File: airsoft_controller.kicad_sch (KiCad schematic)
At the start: 31 parts, among them J1 Micro_SD_Card, SW1 MEMBRANE, SW2 MEMBRANE, SW3 MECH_SW, SW4 MEMBRANE, SW5 MEMBRANE, SW6 MEMBRANE, SW7 MEMBRANE, U1 CP2102N-Axx-xQFN20, U2 ESP32-S3-WROOM-1, U3 74HC595, U8 SN74HCS165

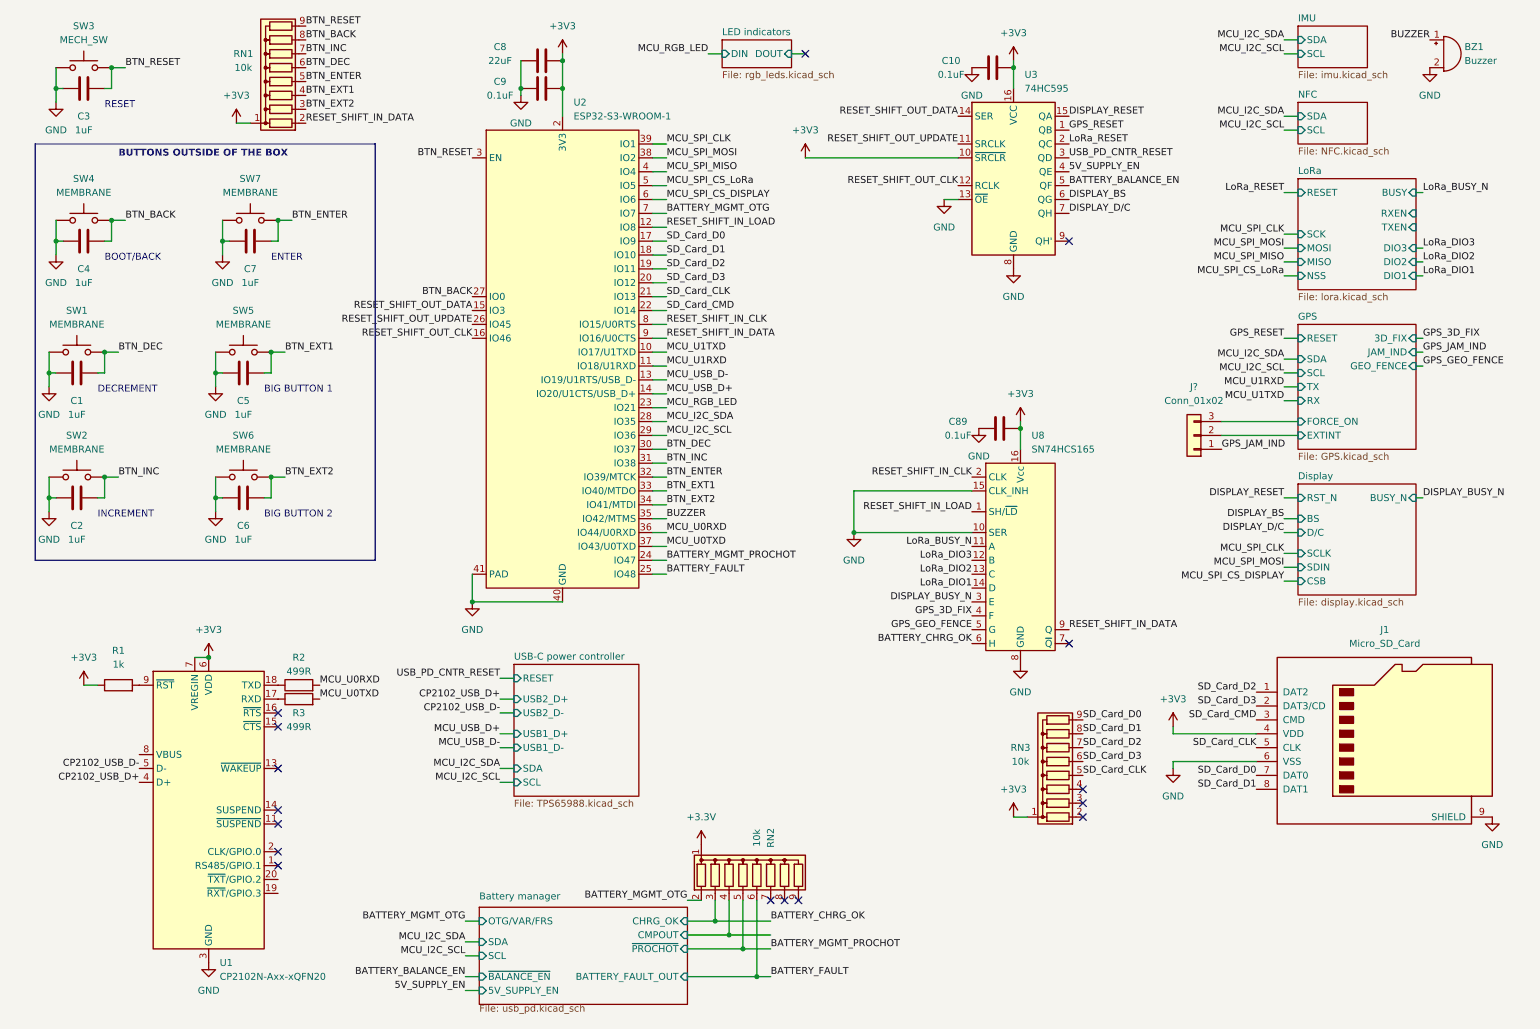
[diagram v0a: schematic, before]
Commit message: minor optimized pinassignement, added capacitors, added connectors
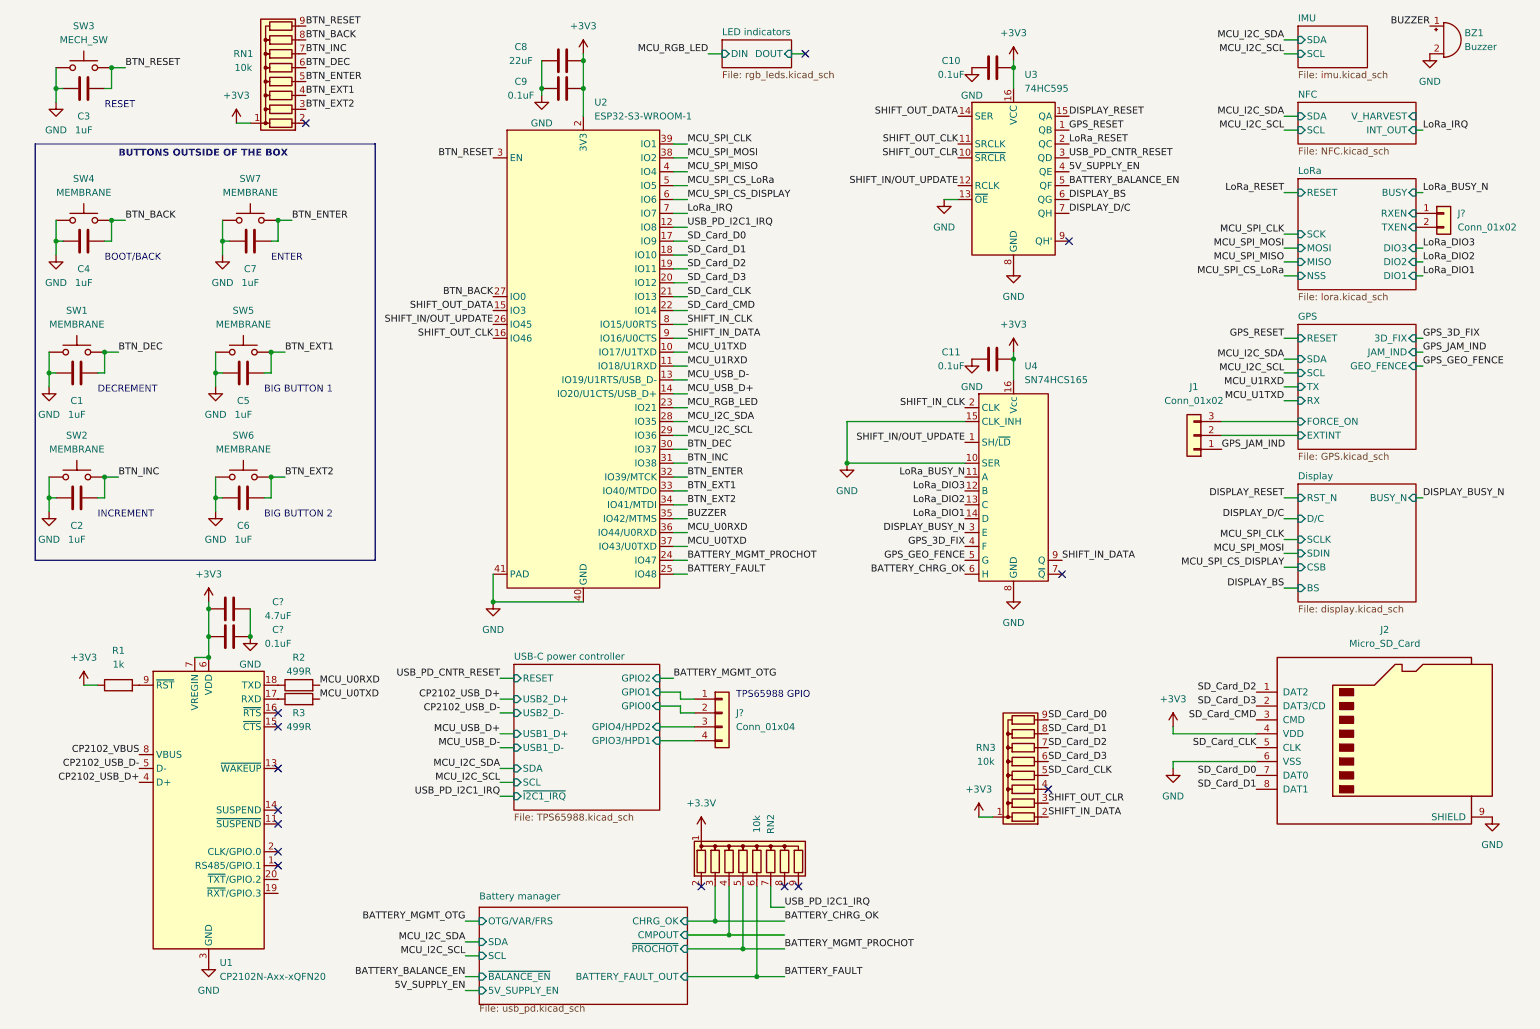
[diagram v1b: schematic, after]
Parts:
- added C?: 0.1uF, symbol Device:C
- added C?: 4.7uF, symbol Device:C
- added J?: Conn_01x02, symbol Connector_Generic:Conn_01x02
- added J?: Conn_01x04, symbol Connector_Generic:Conn_01x04
- gave numbers to parts that had none: 1
- renumbered C89 to C11, J1 to J2, U8 to U4
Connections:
- net +3V3: now also C?.1, C?.1; no longer U3.10 (~{SRCLR})
- net BATTERY_MGMT_OTG: no longer RN2.2 (R1), U2.7 (IO7)
- net GND: now also C?.2, C?.2
- net LoRa/RXEN: now also J?.1 (Pin_1)
- net LoRa/TXEN: now also J?.2 (Pin_2)
- net CP2102_VBUS: now reaches U1.8 (VBUS)
- net SHIFT_IN_DATA: now reaches RN3.2 (R1)
- net SHIFT_IN_DATA: now also U2.9 (IO16/U0CTS), U4.9 (Q)
- net SHIFT_OUT_CLR: now reaches RN3.3 (R2)
- net SHIFT_OUT_CLR: now also U3.10 (~{SRCLR})
- net USB_PD_I2C1_IRQ: now reaches RN2.7 (R6)
- net USB_PD_I2C1_IRQ: now also U2.12 (IO8)
- net RESET_SHIFT_IN_CLK renamed SHIFT_IN_CLK
- removed net RESET_SHIFT_IN_DATA: RN1.2 (R1), U2.9 (IO16/U0CTS), U4.9 (Q)
- net RESET_SHIFT_IN_LOAD renamed SHIFT_IN/OUT_UPDATE
- net SHIFT_IN/OUT_UPDATE: now also U2.26 (IO45), U3.12 (RCLK); no longer U2.12 (IO8)
- net RESET_SHIFT_OUT_CLK renamed SHIFT_OUT_CLK
- net SHIFT_OUT_CLK: now also U3.11 (SRCLK); no longer U3.12 (RCLK)
- net RESET_SHIFT_OUT_DATA renamed SHIFT_OUT_DATA
- removed net RESET_SHIFT_OUT_UPDATE: U2.26 (IO45), U3.11 (SRCLK)
- new net LoRa_IRQ: U2.7 (IO7)
- new net USB-C power controller/GPIO0: J?.2 (Pin_2)
- new net USB-C power controller/GPIO1: J?.1 (Pin_1)
- new net USB-C power controller/GPIO3/HPD1: J?.4 (Pin_4)
- new net USB-C power controller/GPIO4/HPD2: J?.3 (Pin_3)
- no-connect marks 16 -> 15
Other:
- sheet NFC ports: added INT_OUT, V_HARVEST; removed none
- sheet USB-C power controller ports: added GPIO0, GPIO1, GPIO2, GPIO3/HPD1, GPIO4/HPD2, ~{I2C1_IRQ}; removed none
- note added: "TPS65988 GPIO"
- moved on the sheet: BZ1, C11, C8, C9, RN2, RN3, U2, U4

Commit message: PI LC lowpass filter, added CP2012 reset, added connectors
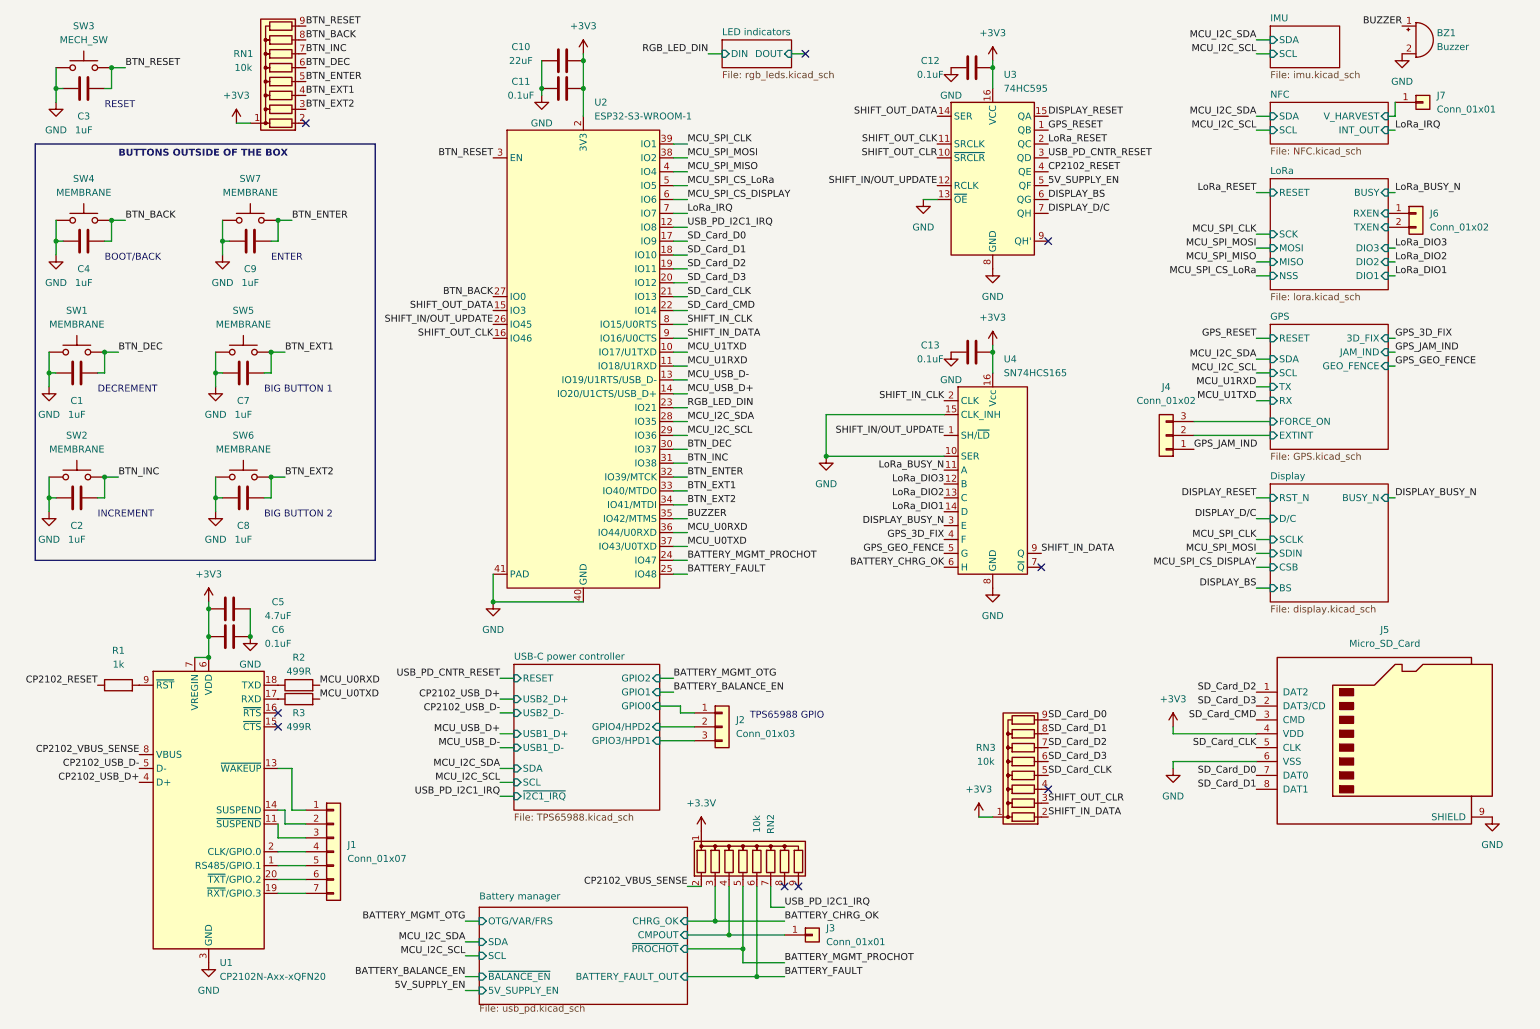
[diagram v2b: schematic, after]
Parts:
- removed J?: Conn_01x04, symbol Connector_Generic:Conn_01x04
- added J1: Conn_01x07, symbol Connector_Generic:Conn_01x07
- added J2: Conn_01x03, symbol Connector_Generic:Conn_01x03
- added J3, J7: Conn_01x01, symbol Connector_Generic:Conn_01x01
- gave numbers to parts that had none: 3
- renumbered C8 to C10, C9 to C11, C10 to C12, C11 to C13, C5 to C7, C6 to C8, C7 to C9, J1 to J4, J2 to J5
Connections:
- net CP2102_VBUS is gone; now on net CP2102_VBUS_SENSE: U1.8 (VBUS)
- net +3V3: no longer R1.1
- net 5V_SUPPLY_EN: now also U3.5 (QF); no longer U3.4 (QE)
- net BATTERY_BALANCE_EN: no longer U3.5 (QF)
- net Battery manager/CMPOUT: now also J3.1 (Pin_1)
- net NFC/V_HARVEST: now also J7.1 (Pin_1)
- net USB-C power controller/GPIO0: now also J2.1 (Pin_1)
- net USB-C power controller/GPIO3/HPD1: now also J2.3 (Pin_3)
- net USB-C power controller/GPIO4/HPD2: now also J2.2 (Pin_2)
- net at U1.1 (RS485/GPIO.1): now also J1.5 (Pin_5)
- net at U1.11 (~{SUSPEND}): now also J1.3 (Pin_3)
- net at U1.13 (~{WAKEUP}): now also J1.1 (Pin_1)
- net at U1.14 (SUSPEND): now also J1.2 (Pin_2)
- net at U1.19 (~{RXT}/GPIO.3): now also J1.7 (Pin_7)
- net at U1.2 (CLK/GPIO.0): now also J1.4 (Pin_4)
- net at U1.20 (~{TXT}/GPIO.2): now also J1.6 (Pin_6)
- net CP2102_VBUS_SENSE: now reaches RN2.2 (R1)
- net MCU_RGB_LED renamed RGB_LED_DIN
- new net CP2102_RESET: R1.1, U3.4 (QE)
- no-connect marks 15 -> 9
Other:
- moved on the sheet: BZ1, C12, C13, J4, J6, U3, U4

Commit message: datasheet checkout, added couple of capacitors for usb-c, groupd some scheatics
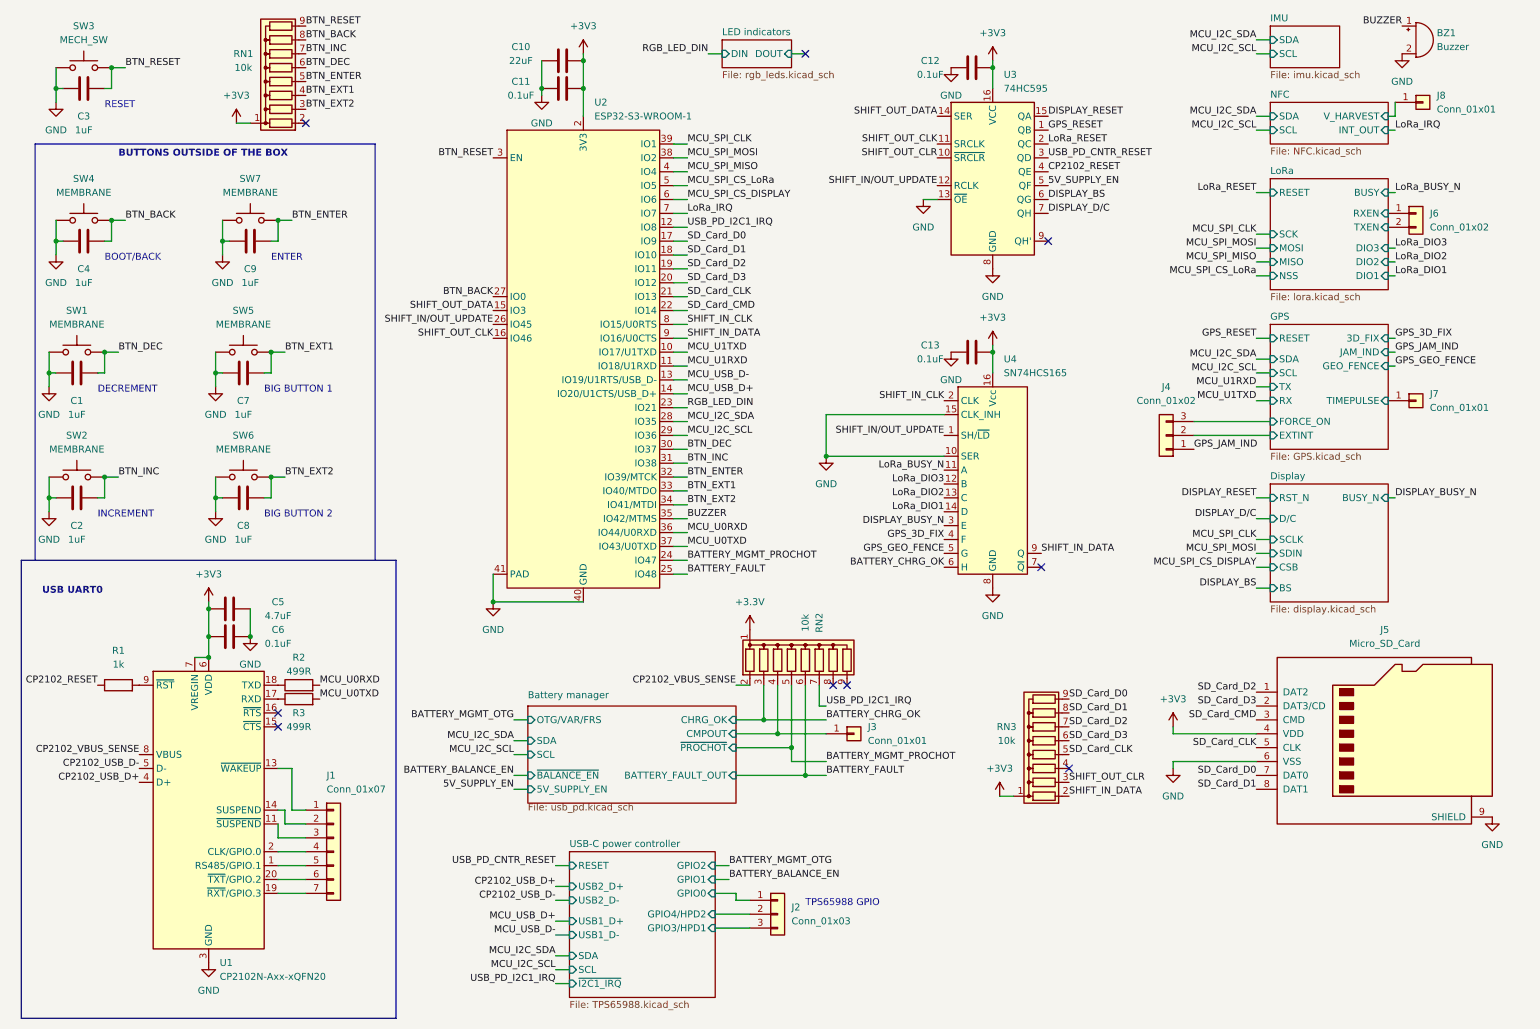
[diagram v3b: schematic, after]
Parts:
- added J7: Conn_01x01, symbol Connector_Generic:Conn_01x01
- renumbered J7 to J8
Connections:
- new net GPS/TIMEPULSE: J7.1 (Pin_1)
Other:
- sheet GPS ports: added TIMEPULSE; removed none
- note added: "USB UART0"
- moved on the sheet: J2, J3, RN2, RN3

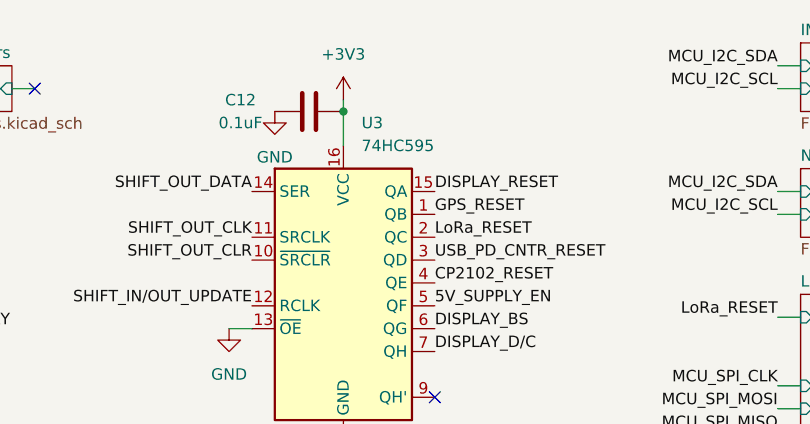
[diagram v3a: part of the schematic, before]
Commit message: added nfc antenna components, added most of footprints
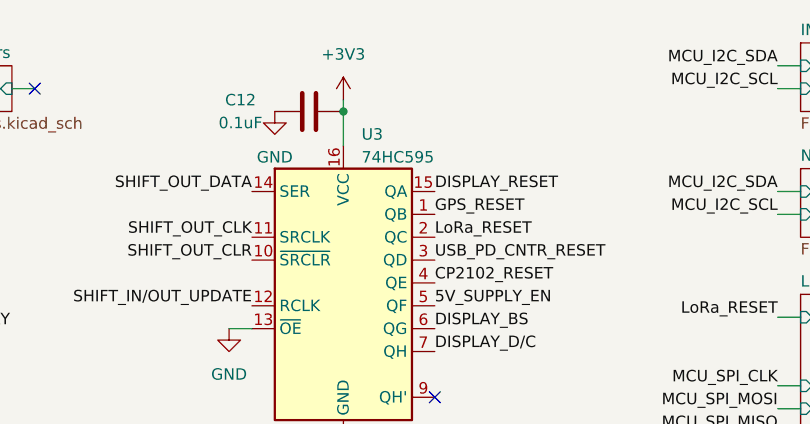
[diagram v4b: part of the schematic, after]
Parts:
- C1, C11, C12, C13, C2, C3, C4, C5, C6, C7, C8, C9: footprint (none) -> Capacitor_SMD:C_0603_1608Metric_Pad1.08x0.95mm_HandSolder
- J1: footprint (none) -> Connector_PinSocket_2.54mm:PinSocket_1x07_P2.54mm_Vertical
- J2: footprint (none) -> Connector_PinSocket_2.54mm:PinSocket_1x03_P2.54mm_Vertical
- J3, J7, J8: footprint (none) -> Connector_PinSocket_2.54mm:PinSocket_1x01_P2.54mm_Vertical
- J4, J6: footprint (none) -> Connector_PinSocket_2.54mm:PinSocket_1x02_P2.54mm_Vertical
- J5: footprint (none) -> airsoft_controller:microSD-W3JA7HH800293
- R1, R2, R3: footprint (none) -> Resistor_SMD:R_0603_1608Metric_Pad0.98x0.95mm_HandSolder
- SW3: footprint (none) -> airsoft_controller:SWITCH_TL3315NF250Q
- U4: footprint (none) -> Package_SO:TSSOP-16_4.4x5mm_P0.65mm

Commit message: schematic creation
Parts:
- removed C10: 22uF, symbol Device:C
- removed J7, J8: Conn_01x01, Connector_PinSocket_2.54mm:PinSocket_1x01_P2.54mm_Vertical, symbol Connector_Generic:Conn_01x01
- removed R2, R3: 499R, Resistor_SMD:R_0603_1608Metric_Pad0.98x0.95mm_HandSolder, symbol Device:R
- added C10: 22uF, Capacitor_SMD:CP_Elec_5x5.3, symbol Device:C_Polarized
- added J3, J7: Conn_01x03, Connector_PinSocket_2.54mm:PinSocket_1x03_P2.54mm_Vertical, symbol Connector_Generic:Conn_01x03
- BZ1: footprint (none) -> airsoft_controller:Buzzer
- C1, C2, C3, C4, C7, C8, C9: value 1uF -> 0.1uF
- J5: renamed from J4; value Conn_01x02 -> Conn_01x03; footprint Connector_PinSocket_2.54mm:PinSocket_1x02_P2.54mm_Vertical -> Connector_PinSocket_2.54mm:PinSocket_1x04_P2.54mm_Vertical; symbol Connector_Generic:Conn_01x03 -> Connector_Generic:Conn_01x04
- J6: renamed from J5; symbol Connector:Micro_SD_Card -> Connector:Micro_SD_Card_Det
- SW1, SW2, SW4, SW5, SW6, SW7: footprint (none) -> airsoft_controller:SW_rubber_membrane_for_led
- SW3: symbol Switch:SW_Push -> Switch:SW_MEC_5G
- U1: footprint Package_DFN_QFN:SiliconLabs_QFN-20-1EP_3x3mm_P0.5mm -> Package_DFN_QFN:SiliconLabs_QFN-20-1EP_3x3mm_P0.5mm_EP1.8x1.8mm
- U3: footprint (none) -> Package_SO:TSSOP-16_4.4x5mm_P0.65mm
- renumbered J3 to J4, J6 to J8
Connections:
- net +3V3: now also C10.1
- net BTN_RESET: now also RN3.9 (R8), SW3.3 (B), SW3.4 (B); no longer RN1.9 (R8), SW3.2
- net GND: now also J6.10 (DET_A), J6.11 (SHIELD), SW3.2 (A), C10.2, J3.3 (Pin_3); no longer J6.9 (SHIELD)
- net GPS/EXTINT: now also J5.3 (Pin_3); no longer J5.2 (Pin_2)
- net GPS/FORCE_ON: now also J5.4 (Pin_4); no longer J5.3 (Pin_3)
- net GPS_JAM_IND: now also J5.2 (Pin_2); no longer J5.1 (Pin_1)
- net LED indicators/DOUT: now also J3.2 (Pin_2)
- net MCU_U0RXD: now also U1.18 (TXD)
- net MCU_U0TXD: now also U1.17 (RXD)
- net NFC/V_HARVEST: now also J7.1 (Pin_1)
- net SD_Card_CLK: now also RN3.6 (R5); no longer RN3.5 (R4)
- net SD_Card_D0: now also RN3.7 (R6); no longer RN3.9 (R8)
- net SD_Card_D2: now also RN3.4 (R3); no longer RN3.7 (R6)
- net SD_Card_D3: now also RN3.5 (R4); no longer RN3.6 (R5)
- new net +5V: J3.1 (Pin_1)
- new net GPS_TIMEPULSE: J5.1 (Pin_1)
- new net NFC/EXT_AC0: J7.2 (Pin_2)
- new net NFC/EXT_AC1: J7.3 (Pin_3)
- no-connect marks 9 -> 8
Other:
- sheet NFC ports: added EXT_AC0, EXT_AC1; removed none
- moved on the sheet: J8
